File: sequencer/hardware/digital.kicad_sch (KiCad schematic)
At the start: 63 parts, among them J10 JST_4-pin_male, J11 Conn_01x03, J12 Conn_01x03, J13 Conn_01x03, J14 Conn_01x03, J15 JST_4-pin_male, J16 JST_4-pin_male, J17 Conn_01x03, J7 Conn_01x03_Male, J8 Conn_01x03_Male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

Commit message: Add ground planes
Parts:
- added R38, R39: 10k, Resistor_SMD:R_0603_1608Metric_Pad0.98x0.95mm_HandSolder, symbol Device:R
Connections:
- net GNDD: now also R38.2, R39.2
- net GPIO4_BTN0: now also R38.1
- net GPIO5_BTN1: now also R39.1
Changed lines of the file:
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@@
   (junction (at 288.29 36.83) (diameter 0) (color 0 0 0 0)
   )
+  (junction (at 46.99 160.02) (diameter 0) (color 0 0 0 0)
+  )
   (junction (at 44.45 33.02) (diameter 0) (color 0 0 0 0)
   )
@@
   )
   (junction (at 44.45 44.45) (diameter 0) (color 0 0 0 0)
+  )
+  (junction (at 46.99 184.15) (diameter 0) (color 0 0 0 0)
   )
   (junction (at 30.48 116.84) (diameter 0) (color 0 0 0 0)
@@
     (stroke (width 0) (type default) (color 0 0 0 0))
   )
+  (wire (pts (xy 39.37 181.61) (xy 39.37 184.15))
+    (stroke (width 0) (type default) (color 0 0 0 0))
+  )
   (wire (pts (xy 212.09 36.83) (xy 212.09 40.64))
     (stroke (width 0) (type default) (color 0 0 0 0))
@@
   )
   (wire (pts (xy 200.66 129.54) (xy 190.5 129.54))
+    (stroke (width 0) (type default) (color 0 0 0 0))
+  )
+  (wire (pts (xy 39.37 157.48) (xy 39.37 160.02))
     (stroke (width 0) (type default) (color 0 0 0 0))
   )
@@
   (hierarchical_label "GPIO5_I2C0_SCL" (shape output) (at 271.78 76.2 0)
     (effects (font (size 1.27 1.27)) (justify left))
+  )
+  (symbol (lib_id "Device:R") (at 43.18 160.02 90) (unit 1)
+    (in_bom yes) (on_board yes)
+    (property "Reference" "R38" (id 0) (at 43.18 162.56 90))
+    (property "Value" "10k" (id 1) (at 43.18 160.02 90))
+    (property "Footprint" "Resistor_SMD:R_0603_1608Metric_Pad0.98x0.95mm_HandSolder" (id 2) (at 43.18 161.798 90)
+      (effects (font (size 1.27 1.27)) hide)
+    )
+    (property "Datasheet" "~" (id 3) (at 43.18 160.02 0)
+      (effects (font (size 1.27 1.27)) hide)
+    )
+    (pin "1")
+    (pin "2")
   )
   (symbol (lib_id "Connector:Conn_01x03_Male") (at 95.25 97.79 180) (unit 1)
@@
     (pin "1")
   )
+  (symbol (lib_id "Device:R") (at 43.18 184.15 90) (unit 1)
+    (in_bom yes) (on_board yes)
+    (property "Reference" "R39" (id 0) (at 43.18 186.69 90))
+    (property "Value" "10k" (id 1) (at 43.18 184.15 90))
+    (property "Footprint" "Resistor_SMD:R_0603_1608Metric_Pad0.98x0.95mm_HandSolder" (id 2) (at 43.18 185.928 90)
+      (effects (font (size 1.27 1.27)) hide)
+    )
+    (property "Datasheet" "~" (id 3) (at 43.18 184.15 0)
+      (effects (font (size 1.27 1.27)) hide)
+    )
+    (pin "1")
+    (pin "2")
+  )
   (symbol (lib_id "Device:C") (at 107.95 38.1 0) (unit 1)

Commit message: Route digital domain
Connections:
- net GPIO10_ENC21: now also U8.14 (GPIO11); no longer U8.13 (GPIO10)
- net GPIO16_NEXTPRSNT: now also U8.34 (GPIO22); no longer U8.18 (GPIO15)
- net GPIO9_ENC20: now also U8.13 (GPIO10); no longer U8.12 (GPIO9)

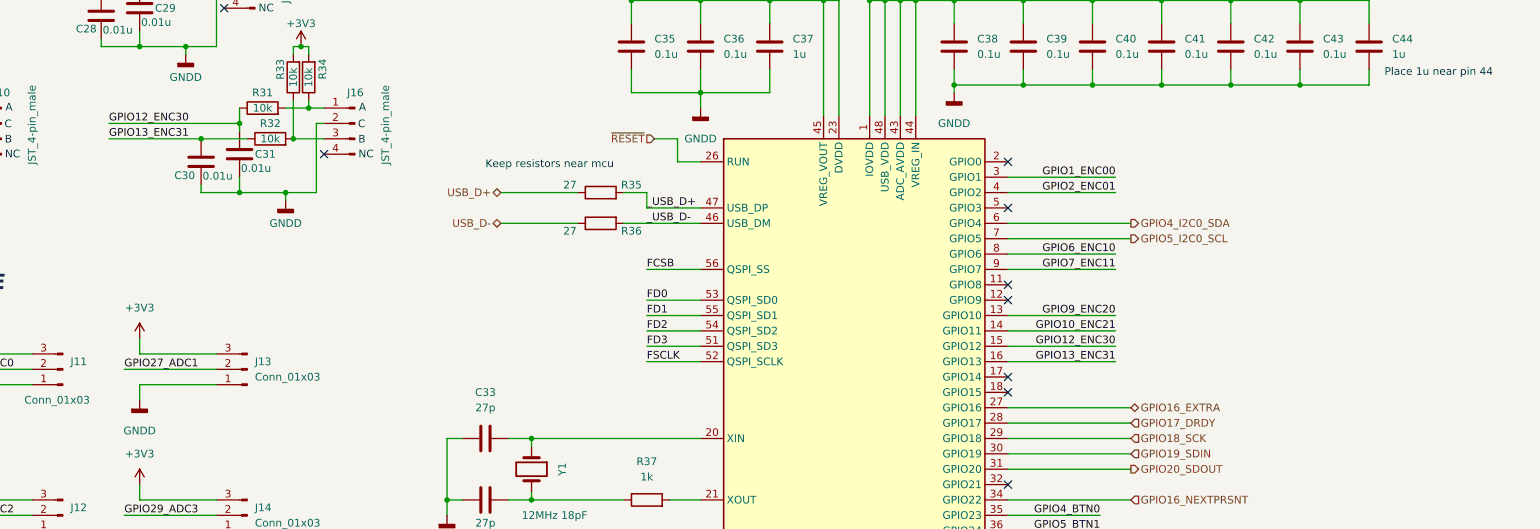
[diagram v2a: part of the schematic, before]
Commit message: Add OLED header
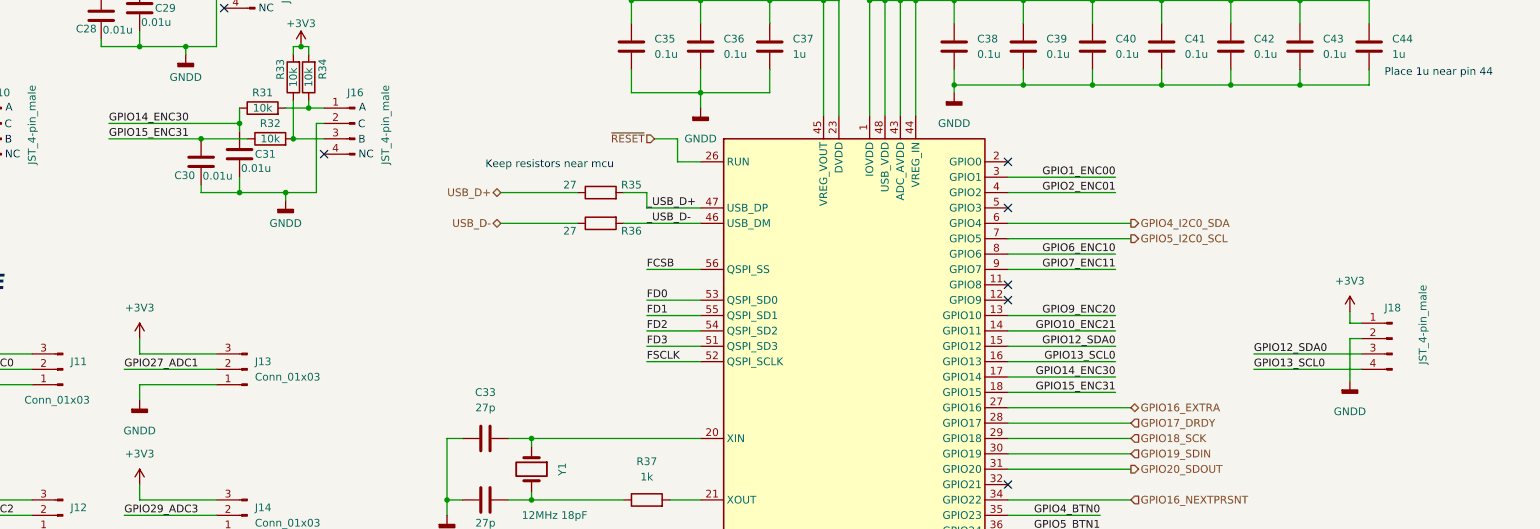
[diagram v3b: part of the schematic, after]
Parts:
- added J18: JST_4-pin_male, Connector_JST:JST_PH_B4B-PH-K_1x04_P2.00mm_Vertical, symbol Connector:Conn_01x04_Male
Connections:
- net +3V3: now also J18.1 (Pin_1)
- net GNDD: now also J18.2 (Pin_2)
- net GPIO14_ENC30: now reaches U8.17 (GPIO14)
- net GPIO14_ENC30: now also C31.1, R31.1
- net GPIO15_ENC31: now reaches U8.18 (GPIO15)
- net GPIO15_ENC31: now also C30.1, R32.1
- removed net GPIO12_ENC30: C31.1, R31.1, U8.15 (GPIO12)
- removed net GPIO13_ENC31: C30.1, R32.1, U8.16 (GPIO13)
- new net GPIO12_SDA0: J18.3 (Pin_3), U8.15 (GPIO12)
- new net GPIO13_SCL0: J18.4 (Pin_4), U8.16 (GPIO13)
- no-connect marks 12 -> 10

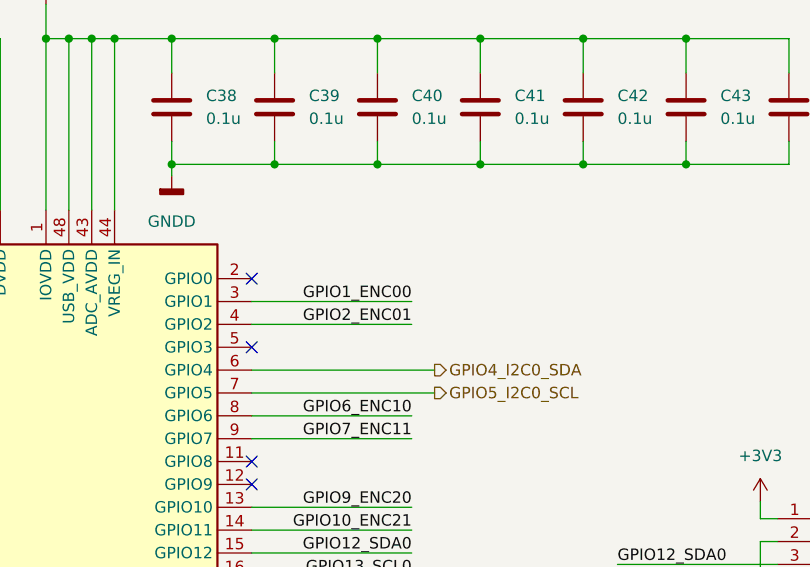
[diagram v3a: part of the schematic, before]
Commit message: Add board notches; align mounting holes
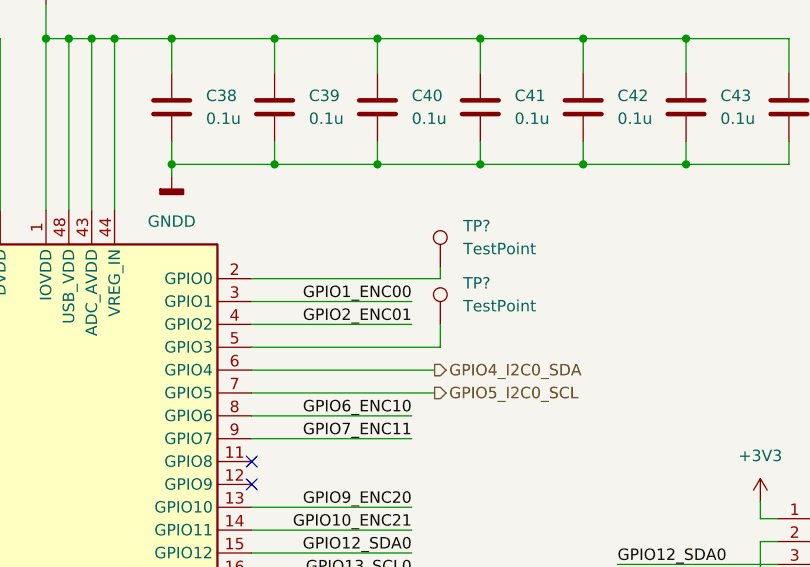
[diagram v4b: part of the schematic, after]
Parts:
- added TP? (x2): TestPoint, TestPoint:TestPoint_Pad_D1.5mm, symbol Connector:TestPoint
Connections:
- net at U8.2 (GPIO0): now also TP?.1
- net at U8.5 (GPIO3): now also TP?.1
- no-connect marks 10 -> 8
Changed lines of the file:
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@@
   )
   (no_connect (at 251.46 116.84))
-  (no_connect (at 251.46 71.12))
   (no_connect (at 251.46 83.82))
   (no_connect (at 251.46 86.36))
   (no_connect (at 80.01 62.23))
-  (no_connect (at 251.46 63.5))
   (no_connect (at 138.43 62.23))
   (no_connect (at 58.42 38.1))
@@
     (stroke (width 0) (type default) (color 0 0 0 0))
   )
+  (wire (pts (xy 251.46 71.12) (xy 272.415 71.12))
+    (stroke (width 0) (type default) (color 0 0 0 0))
+  )
   (wire (pts (xy 22.86 33.02) (xy 44.45 33.02))
     (stroke (width 0) (type default) (color 0 0 0 0))
@@
     (stroke (width 0) (type default) (color 0 0 0 0))
   )
+  (wire (pts (xy 272.415 63.5) (xy 251.46 63.5))
+    (stroke (width 0) (type default) (color 0 0 0 0))
+  )
   (wire (pts (xy 140.97 140.97) (xy 140.97 144.78))
     (stroke (width 0) (type default) (color 0 0 0 0))
@@
     (stroke (width 0) (type default) (color 0 0 0 0))
   )
+  (wire (pts (xy 272.415 71.12) (xy 272.415 68.58))
+    (stroke (width 0) (type default) (color 0 0 0 0))
+  )
   (wire (pts (xy 107.95 124.46) (xy 107.95 127))
     (stroke (width 0) (type default) (color 0 0 0 0))
@@
   )
   (wire (pts (xy 266.7 124.46) (xy 251.46 124.46))
+    (stroke (width 0) (type default) (color 0 0 0 0))
+  )
+  (wire (pts (xy 272.415 62.23) (xy 272.415 63.5))
     (stroke (width 0) (type default) (color 0 0 0 0))
   )
@@
     )
     (property "Datasheet" "" (id 3) (at 52.07 45.72 0)
+      (effects (font (size 1.27 1.27)) hide)
+    )
+    (pin "1")
+  )
+  (symbol (lib_id "Connector:TestPoint") (at 272.415 68.58 0) (unit 1)
+    (in_bom yes) (on_board yes) (fields_autoplaced)
+    (property "Reference" "TP?" (id 0) (at 274.955 64.0079 0)
+      (effects (font (size 1.27 1.27)) (justify left))
+    )
+    (property "Value" "TestPoint" (id 1) (at 274.955 66.5479 0)
+      (effects (font (size 1.27 1.27)) (justify left))
+    )
+    (property "Footprint" "TestPoint:TestPoint_Pad_D1.5mm" (id 2) (at 277.495 68.58 0)
+      (effects (font (size 1.27 1.27)) hide)
+    )
+    (property "Datasheet" "~" (id 3) (at 277.495 68.58 0)
       (effects (font (size 1.27 1.27)) hide)
     )
@@
       (effects (font (size 1.27 1.27)) hide)
     )
+    (pin "1")
+  )
+  (symbol (lib_id "Connector:TestPoint") (at 272.415 62.23 0) (unit 1)
+    (in_bom yes) (on_board yes) (fields_autoplaced)
+    (property "Reference" "TP?" (id 0) (at 274.955 57.6579 0)
+      (effects (font (size 1.27 1.27)) (justify left))
+    )
+    (property "Value" "TestPoint" (id 1) (at 274.955 60.1979 0)
+      (effects (font (size 1.27 1.27)) (justify left))
+    )
+    (property "Footprint" "TestPoint:TestPoint_Pad_D1.5mm" (id 2) (at 277.495 62.23 0)
+      (effects (font (size 1.27 1.27)) hide)
+    )
+    (property "Datasheet" "~" (id 3) (at 277.495 62.23 0)
+      (effects (font (size 1.27 1.27)) hide)
+    )

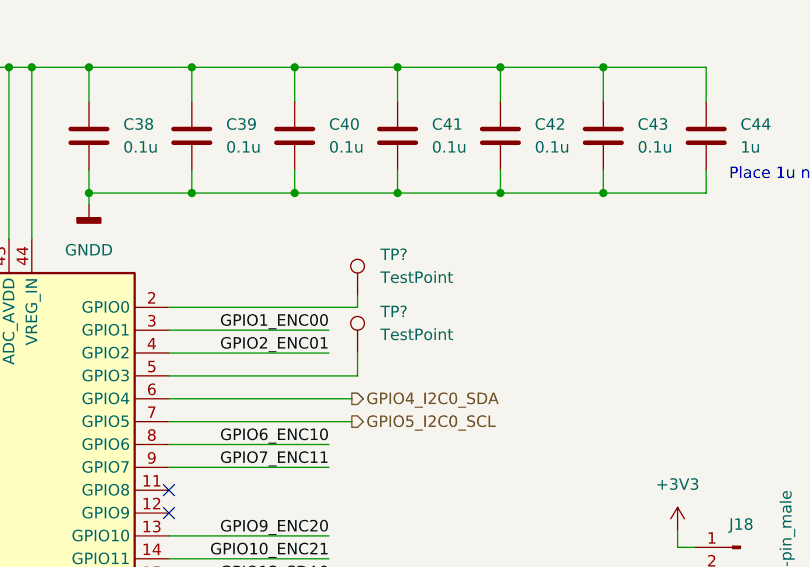
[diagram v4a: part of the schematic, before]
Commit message: Implement star grounding
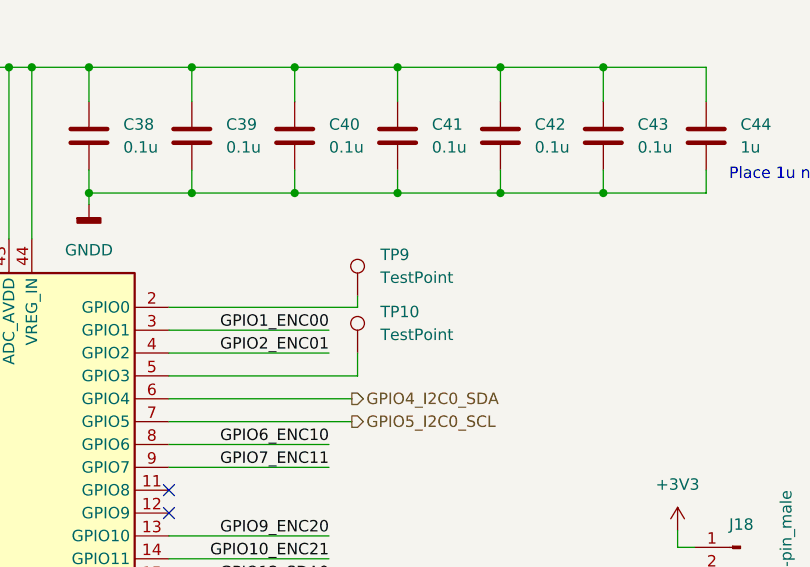
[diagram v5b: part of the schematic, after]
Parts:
- gave numbers to parts that had none: 2
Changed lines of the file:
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@@
   (symbol (lib_id "Connector:TestPoint") (at 272.415 68.58 0) (unit 1)
     (in_bom yes) (on_board yes) (fields_autoplaced)
-    (property "Reference" "TP?" (id 0) (at 274.955 64.0079 0)
+    (property "Reference" "TP10" (id 0) (at 274.955 64.0079 0)
       (effects (font (size 1.27 1.27)) (justify left))
     )
@@
   (symbol (lib_id "Connector:TestPoint") (at 272.415 62.23 0) (unit 1)
     (in_bom yes) (on_board yes) (fields_autoplaced)
-    (property "Reference" "TP?" (id 0) (at 274.955 57.6579 0)
-      (effects (font (size 1.27 1.27)) (justify left))
-    )
+    (property "Reference" "TP9" (id 0) (at 274.955 57.6579 0)
+      (effects (font (size 1.27 1.27)) (justify left))
+    )

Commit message: Add button debounce passives
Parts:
- added C? (x4): 0.01u, Capacitor_SMD:C_0805_2012Metric_Pad1.18x1.45mm_HandSolder, symbol Device:C
- added R? (x6): 10k, Resistor_SMD:R_0603_1608Metric_Pad0.98x0.95mm_HandSolder, symbol Device:R
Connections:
- net +3V3: now also R?.2, R?.2
- net GNDD: now also C?.2, C?.2, C?.2, C?.2
- net GPIO4_BTN0: now also C?.1, R?.1; no longer J7.2 (Pin_2), R15.1, R38.1
- net GPIO5_BTN1: now also C?.1, R?.1; no longer J8.2 (Pin_2), R16.1, R39.1
- net at J10.4 (Pin_4): now also R?.1, R?.2
- net at J9.4 (Pin_4): now also R?.1, R?.2
- net GPIO8_ENC0B: now reaches U8.11 (GPIO8)
- net GPIO8_ENC0B: now also C?.1, R?.1
- net GPIO9_ENC2B: now reaches U8.12 (GPIO9)
- net GPIO9_ENC2B: now also C?.1, R?.1
- net GPIO21_EXTRA1: now reaches U8.32 (GPIO21)
- net GPIO16_EXTRA renamed GPIO16_EXTRA0
- new net: J7.2 (Pin_2), R15.1, R38.1, R?.2
- new net: J8.2 (Pin_2), R16.1, R39.1, R?.2
- no-connect marks 8 -> 3
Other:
- note added: "BTN"
- moved on the sheet: C20, C21, C22, C23, C24, C25, C26, C27, C28, C29, C30, C31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

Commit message: Route button debounce passives; bump HW rev to 1.1 (repeat)
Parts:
- gave numbers to parts that had none: 10
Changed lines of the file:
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@@
   (symbol (lib_id "Device:C") (at 117.475 76.2 0) (unit 1)
     (in_bom yes) (on_board yes)
-    (property "Reference" "C?" (id 0) (at 113.03 74.295 0)
+    (property "Reference" "C50" (id 0) (at 113.03 74.295 0)
       (effects (font (size 1.27 1.27)) (justify left))
     )
@@
   (symbol (lib_id "Device:C") (at 256.54 191.135 0) (unit 1)
     (in_bom yes) (on_board yes)
-    (property "Reference" "C?" (id 0) (at 252.1122 193.3913 0)
+    (property "Reference" "C51" (id 0) (at 252.1122 193.3913 0)
       (effects (font (size 1.27 1.27)) (justify left))
     )
@@
   (symbol (lib_id "Device:R") (at 261.62 186.055 90) (unit 1)
     (in_bom yes) (on_board yes)
-    (property "Reference" "R?" (id 0) (at 261.62 183.515 90))
+    (property "Reference" "R44" (id 0) (at 261.62 183.515 90))
     (property "Value" "10k" (id 1) (at 261.62 186.055 90))
     (property "Footprint" "Resistor_SMD:R_0603_1608Metric_Pad0.98x0.95mm_HandSolder" (id 2) (at 261.62 187.833 90)
@@
   (symbol (lib_id "Device:R") (at 75.565 71.12 90) (unit 1)
     (in_bom yes) (on_board yes)
-    (property "Reference" "R?" (id 0) (at 69.85 69.85 90))
+    (property "Reference" "R40" (id 0) (at 69.85 69.85 90))
     (property "Value" "10k" (id 1) (at 75.565 71.12 90))
     (property "Footprint" "Resistor_SMD:R_0603_1608Metric_Pad0.98x0.95mm_HandSolder" (id 2) (at 75.565 72.898 90)
@@
   (symbol (lib_id "power:GNDD") (at 256.54 220.98 0) (unit 1)
     (in_bom yes) (on_board yes) (fields_autoplaced)
-    (property "Reference" "#PWR?" (id 0) (at 256.54 227.33 0)
+    (property "Reference" "#PWR081" (id 0) (at 256.54 227.33 0)
       (effects (font (size 1.27 1.27)) hide)
     )
@@
   (symbol (lib_id "Device:C") (at 46.99 76.835 0) (unit 1)
     (in_bom yes) (on_board yes)
-    (property "Reference" "C?" (id 0) (at 42.545 74.93 0)
+    (property "Reference" "C49" (id 0) (at 42.545 74.93 0)
       (effects (font (size 1.27 1.27)) (justify left))
     )
@@
   (symbol (lib_id "Device:R") (at 261.62 210.185 90) (unit 1)
     (in_bom yes) (on_board yes)
-    (property "Reference" "R?" (id 0) (at 261.62 207.645 90))
+    (property "Reference" "R45" (id 0) (at 261.62 207.645 90))
     (property "Value" "10k" (id 1) (at 261.62 210.185 90))
     (property "Footprint" "Resistor_SMD:R_0603_1608Metric_Pad0.98x0.95mm_HandSolder" (id 2) (at 261.62 211.963 90)
@@
   (symbol (lib_id "power:GNDD") (at 256.54 196.85 0) (unit 1)
     (in_bom yes) (on_board yes) (fields_autoplaced)
-    (property "Reference" "#PWR?" (id 0) (at 256.54 203.2 0)
+    (property "Reference" "#PWR080" (id 0) (at 256.54 203.2 0)
       (effects (font (size 1.27 1.27)) hide)
     )
@@
   (symbol (lib_id "Device:R") (at 80.645 53.34 180) (unit 1)
     (in_bom yes) (on_board yes)
-    (property "Reference" "R?" (id 0) (at 79.375 48.895 90))
+    (property "Reference" "R41" (id 0) (at 79.375 48.895 90))
     (property "Value" "10k" (id 1) (at 80.645 53.34 90))
     (property "Footprint" "Resistor_SMD:R_0603_1608Metric_Pad0.98x0.95mm_HandSolder" (id 2) (at 82.423 53.34 90)
@@
   (symbol (lib_id "Device:C") (at 256.54 215.265 0) (unit 1)
     (in_bom yes) (on_board yes)
-    (property "Reference" "C?" (id 0) (at 252.1122 217.5213 0)
+    (property "Reference" "C52" (id 0) (at 252.1122 217.5213 0)
       (effects (font (size 1.27 1.27)) (justify left))
     )
@@
   (symbol (lib_id "power:+3V3") (at 85.725 95.25 0) (unit 1)
     (in_bom yes) (on_board yes)
-    (property "Reference" "#PWR?" (id 0) (at 85.725 99.06 0)
+    (property "Reference" "#PWR057" (id 0) (at 85.725 99.06 0)
       (effects (font (size 1.27 1.27)) hide)
     )
@@
   (symbol (lib_id "Device:R") (at 151.13 57.15 180) (unit 1)
     (in_bom yes) (on_board yes)
-    (property "Reference" "R?" (id 0) (at 149.86 52.705 90))
+    (property "Reference" "R43" (id 0) (at 149.86 52.705 90))
     (property "Value" "10k" (id 1) (at 151.13 57.15 90))
     (property "Footprint" "Resistor_SMD:R_0603_1608Metric_Pad0.98x0.95mm_HandSolder" (id 2) (at 152.908 57.15 90)
@@
   (symbol (lib_id "Device:R") (at 146.05 71.12 90) (unit 1)
     (in_bom yes) (on_board yes)
-    (property "Reference" "R?" (id 0) (at 140.97 69.85 90))
+    (property "Reference" "R42" (id 0) (at 140.97 69.85 90))
     (property "Value" "10k" (id 1) (at 146.05 71.12 90))
     (property "Footprint" "Resistor_SMD:R_0603_1608Metric_Pad0.98x0.95mm_HandSolder" (id 2) (at 146.05 72.898 90)
